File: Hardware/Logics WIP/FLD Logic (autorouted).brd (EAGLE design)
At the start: 62.2 x 33 mm, 86 parts

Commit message: 
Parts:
- removed H1, H2, H3, H4: MOUNT-HOLE3.3, holes:3,3
- moved C1 0.95 mm to (52.1, 4.45)
- moved C11 0.95 mm to (20.3, 10.8)
- moved C12 0.95 mm to (27.0, 9.21)
- moved C13 0.95 mm to (33.0, 10.8)
- moved C14 0.95 mm to (39.7, 9.21)
- moved C15 0.95 mm to (45.7, 10.8)
- moved C16 0.95 mm to (52.4, 9.21)
- moved C17 0.95 mm to (52.1, 17.1)
- moved C18 0.95 mm to (46.0, 15.6)
- moved C19 0.95 mm to (39.4, 17.1)
- moved C2 0.95 mm to (46.0, 2.86), turned to 180 degrees
- moved C20 0.95 mm to (33.3, 15.6)
- moved C21 0.95 mm to (26.7, 17.1)
- moved C22 0.95 mm to (20.6, 15.6)
- moved C23 0.95 mm to (14.0, 17.1)
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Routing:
- net +5V: track 460.1 -> 431.1 mm, vias 39 -> 40
- net DOUT: track 53.1 -> 28.5 mm, vias 3 -> 1
- net GND: track 360.7 -> 343.3 mm, vias 41 -> 40
- net N$36: track 24.8 -> 13.2 mm, vias 2 -> 0
- net N$37: track 13.2 -> 18.9 mm, vias 0 -> 2
- net N$7: track 12.2 -> 7.75 mm, vias 2 -> 0
- net N$6: track 11.5 -> 15.4 mm
- net N$25: track 12.5 -> 9.08 mm
- net N$11: track 18.7 -> 16.1 mm, vias 2 -> 0
- net N$34: track 7.79 -> 10.1 mm
- net N$8: track 11.0 -> 12.6 mm, vias 2 -> 0
- net N$15: track 12.5 -> 11.2 mm, vias 0 -> 2
- net N$19: track 17.4 -> 16.1 mm, vias 2 -> 0
- net N$20: track 13.2 -> 14.4 mm, vias 0 -> 2
- net N$26: track 12.4 -> 11.2 mm, vias 0 -> 2
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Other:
- board size 62.2 x 33 mm -> 61.6 x 33 mm
- board text added: "+ -"

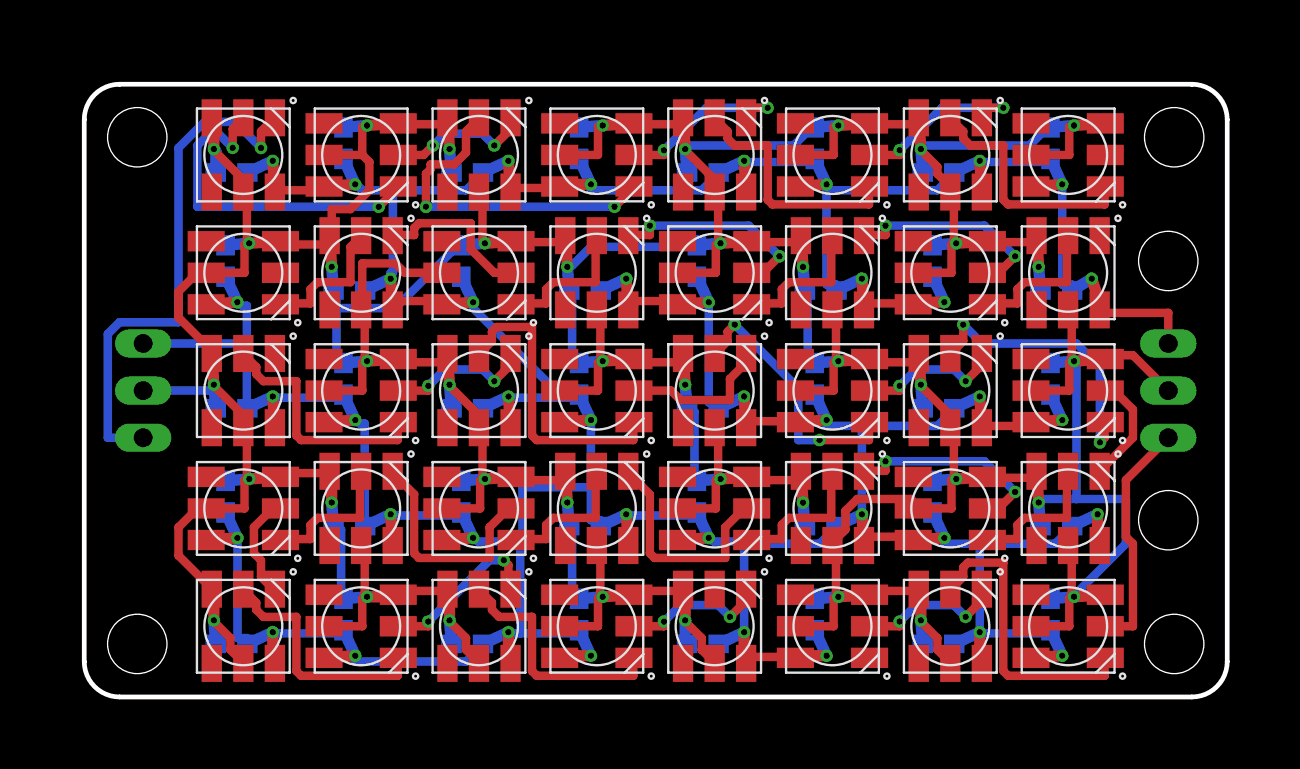
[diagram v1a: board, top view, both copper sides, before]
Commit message: 
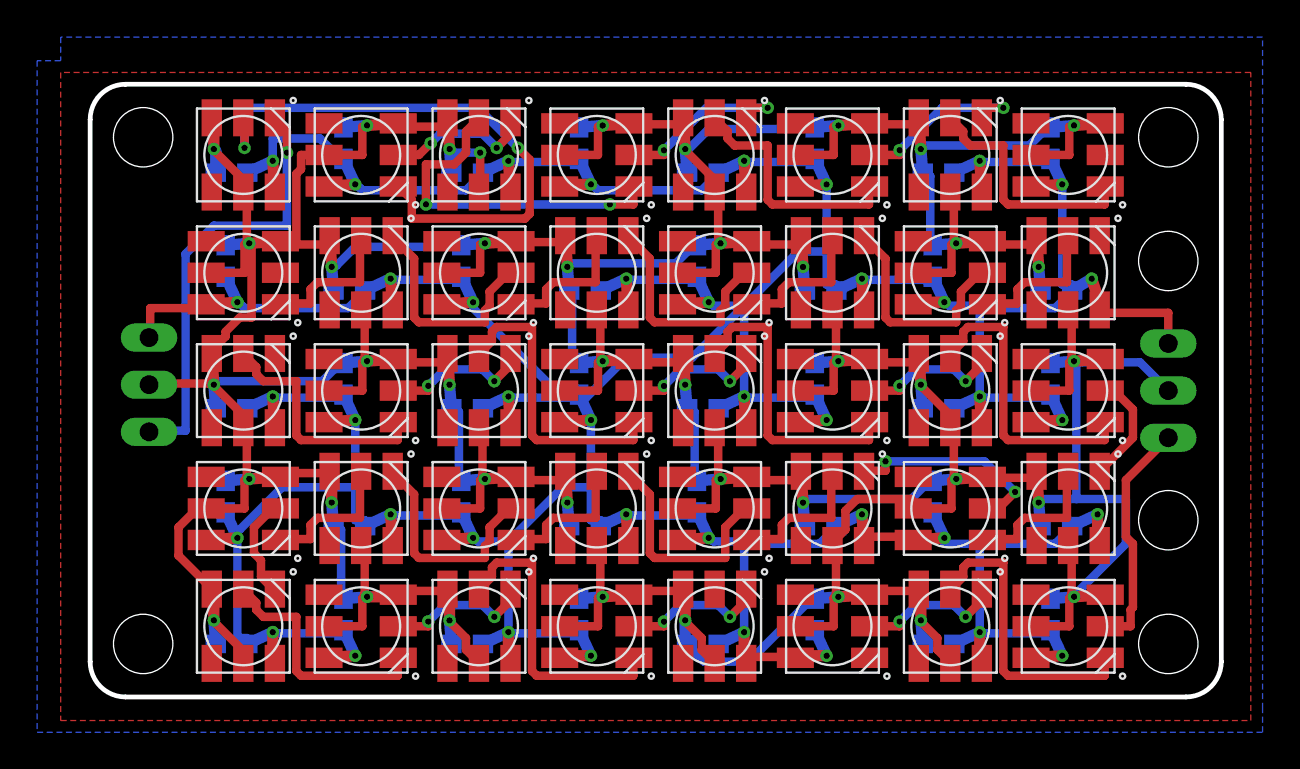
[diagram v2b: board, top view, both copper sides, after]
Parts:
- added U$1: (no value), rseries:RSERIES-OSHW-LOGO-SMALL
- moved OUT 0.45 mm to (3.49, 16.8)
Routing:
- net +5V: track 431.1 -> 445.4 mm, vias 40 -> 41
- net N$37: track 18.9 -> 31.7 mm
- net GND: track 343.3 -> 355.3 mm
- net DOUT: track 28.5 -> 23.7 mm
- net N$25: track 9.08 -> 12.4 mm
- net N$2: track 13.2 -> 16.1 mm
- net N$20: track 14.4 -> 16.1 mm, vias 2 -> 0
- net N$30: track 11.2 -> 12.4 mm, vias 2 -> 0
- net N$26: track 11.2 -> 12.4 mm, vias 2 -> 0
- net N$5: track 9.05 -> 7.92 mm
- net N$6: track 15.4 -> 16.1 mm, vias 2 -> 0
- net N$18: track 8.26 -> 7.92 mm, vias 0 -> 2
- added copper zone on layer 1, net GND
- added copper zone on layer 16, net GND
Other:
- board size 61.6 x 33 mm -> 61 x 33 mm
- board text added: "`VULCAN' FRONT LOGIC DISPLAY 2013-08-28"

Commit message: 
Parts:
- moved U$1 0.32 mm to (6.99, 28.3)
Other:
- board text added: "PROTOTYPE1"
- board text added: "`VULCAN' FRONT LOGIC DISPLAY : 2013-08-28"
- board text removed: "`VULCAN' FRONT LOGIC DISPLAY 2013-08-28"
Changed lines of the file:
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@@
 <setting verticaltext="up"/>
 </settings>
-<grid distance="0.025" unitdist="inch" unit="inch" style="lines" multiple="1" display="yes" altdistance="0.025" altunitdist="inch" altunit="inch"/>
+<grid distance="0.0125" unitdist="inch" unit="inch" style="lines" multiple="1" display="yes" altdistance="0.025" altunitdist="inch" altunit="inch"/>
 <layers>
 <layer number="1" name="Top" color="4" fill="1" visible="yes" active="yes"/>
@@
 <layer number="116" name="Patch_BOT" color="9" fill="4" visible="yes" active="yes"/>
 <layer number="121" name="_tsilk" color="7" fill="1" visible="yes" active="yes"/>
-<layer number="122" name="_bsilk" color="7" fill="1" visible="yes" active="yes"/>
+<layer number="122" name="bSilk" color="7" fill="1" visible="yes" active="yes"/>
 <layer number="123" name="tTestmark" color="7" fill="1" visible="yes" active="yes"/>
 <layer number="124" name="bTestmark" color="7" fill="1" visible="yes" active="yes"/>
@@
 <layer number="132" name="bAdjust" color="7" fill="1" visible="yes" active="yes"/>
 <layer number="144" name="Drill_legend" color="7" fill="1" visible="yes" active="yes"/>
-<layer number="150" name="Notes" color="7" fill="1" visible="yes" active="yes"/>
 <layer number="151" name="HeatSink" color="7" fill="1" visible="yes" active="yes"/>
 <layer number="153" name="FabDoc1" color="6" fill="1" visible="no" active="no"/>
@@
 <board>
 <plain>
-<wire x1="0.3175" y1="1.905" x2="0.3175" y2="31.115" width="0.254" layer="20"/>
-<wire x1="0.3175" y1="31.115" x2="2.2225" y2="33.02" width="0.254" layer="20" curve="-90"/>
-<wire x1="2.2225" y1="33.02" x2="59.3725" y2="33.02" width="0.254" layer="20"/>
-<wire x1="59.3725" y1="33.02" x2="61.2775" y2="31.115" width="0.254" layer="20" curve="-90"/>
-<wire x1="61.2775" y1="31.115" x2="61.2775" y2="1.905" width="0.254" layer="20"/>
-<wire x1="61.2775" y1="1.905" x2="59.3725" y2="0" width="0.254" layer="20" curve="-90"/>
-<wire x1="59.3725" y1="0" x2="2.2225" y2="0" width="0.254" layer="20"/>
-<wire x1="2.2225" y1="0" x2="0.3175" y2="1.905" width="0.254" layer="20" curve="-90"/>
+<wire x1="0.3175" y1="1.905" x2="0.3175" y2="31.115" width="0" layer="20"/>
+<wire x1="0.3175" y1="31.115" x2="2.2225" y2="33.02" width="0" layer="20" curve="-90"/>
+<wire x1="2.2225" y1="33.02" x2="59.3725" y2="33.02" width="0" layer="20"/>
+<wire x1="59.3725" y1="33.02" x2="61.2775" y2="31.115" width="0" layer="20" curve="-90"/>
+<wire x1="61.2775" y1="31.115" x2="61.2775" y2="1.905" width="0" layer="20"/>
+<wire x1="61.2775" y1="1.905" x2="59.3725" y2="0" width="0" layer="20" curve="-90"/>
+<wire x1="59.3725" y1="0" x2="2.2225" y2="0" width="0" layer="20"/>
+<wire x1="2.2225" y1="0" x2="0.3175" y2="1.905" width="0" layer="20" curve="-90"/>
 <hole x="58.42" y="30.1625" drill="3.2"/>
 <hole x="58.42" y="2.8575" drill="3.2"/>
@@
 <text x="61.2775" y="19.84375" size="1.397" layer="26" font="vector" rot="MR270">+ -</text>
 <text x="1.905" y="20.16125" size="1.397" layer="26" font="vector" rot="MR270">+ -</text>
-<text x="26.9875" y="25.4" size="1.016" layer="122" font="vector" rot="MR0" align="center">`VULCAN' FRONT LOGIC DISPLAY
-2013-08-28</text>
+<text x="24.13" y="32.0675" size="1.016" layer="26" font="vector" rot="MR0" align="center">`VULCAN' FRONT LOGIC DISPLAY : 2013-08-28</text>
+<polygon width="0" layer="26">
+<vertex x="16.4465" y="19.177"/>
+<vertex x="16.9545" y="15.875"/>
+<vertex x="18.2245" y="12.827"/>
+<vertex x="18.4785" y="11.811"/>
+<vertex x="18.9865" y="11.303"/>
+<vertex x="19.7485" y="11.557"/>
+<vertex x="20.0025" y="12.319"/>
+<vertex x="18.7325" y="15.367"/>
+<vertex x="17.9705" y="17.145"/>
+<vertex x="17.7165" y="19.177"/>
+<vertex x="18.2245" y="20.701"/>
+<vertex x="19.4945" y="20.955"/>
+<vertex x="20.7645" y="20.193"/>
+<vertex x="21.7805" y="18.923"/>
+<vertex x="22.2885" y="18.161"/>
+<vertex x="23.0505" y="18.415"/>
+<vertex x="23.3045" y="19.177"/>
+<vertex x="23.0505" y="20.193"/>
+<vertex x="22.0345" y="21.463"/>
+<vertex x="21.0185" y="22.225"/>
+<vertex x="20.0025" y="22.479"/>
+<vertex x="18.2245" y="22.225"/>
+<vertex x="16.9545" y="20.955"/>
+</polygon>
+<polygon width="0" layer="26">
+<vertex x="28.1305" y="3.175"/>
+<vertex x="27.6225" y="2.667"/>
+<vertex x="26.3525" y="2.413"/>
+<vertex x="23.8125" y="2.413"/>
+<vertex x="23.0505" y="2.667"/>
+<vertex x="22.2885" y="2.413"/>
+<vertex x="22.0345" y="1.905"/>
+<vertex x="22.2885" y="1.397"/>
+<vertex x="23.3045" y="1.143"/>
+<vertex x="27.1145" y="1.651"/>
+<vertex x="28.8925" y="2.413"/>
+<vertex x="29.6545" y="3.683"/>
+<vertex x="29.4005" y="4.953"/>
+<vertex x="28.6385" y="6.223"/>
+<vertex x="26.6065" y="8.001"/>
+<vertex x="26.0985" y="8.509"/>
+<vertex x="24.8285" y="10.287"/>
+<vertex x="23.8125" y="12.573"/>
+<vertex x="23.3045" y="14.605"/>
+<vertex x="23.3045" y="16.637"/>
+<vertex x="22.7965" y="16.891"/>
+<vertex x="22.0345" y="16.383"/>
+<vertex x="21.7805" y="15.113"/>
+<vertex x="22.0345" y="12.827"/>
+<vertex x="23.0505" y="9.779"/>
+<vertex x="24.5745" y="7.493"/>
+<vertex x="27.1145" y="4.953"/>
+</polygon>
+<polygon width="0" layer="26">
+<vertex x="9.5885" y="13.335"/>
+<vertex x="10.0965" y="12.319"/>
+<vertex x="11.1125" y="12.065"/>
+<vertex x="11.8745" y="10.287"/>
+<vertex x="12.1285" y="9.525"/>
+<vertex x="11.6205" y="8.763"/>
+<vertex x="10.3505" y="7.493"/>
+<vertex x="9.5885" y="6.985"/>
+<vertex x="8.3185" y="5.461"/>
+<vertex x="7.8105" y="3.683"/>
+<vertex x="8.3185" y="2.413"/>
+<vertex x="9.5885" y="1.905"/>
+<vertex x="12.1285" y="2.159"/>
+<vertex x="12.8905" y="2.413"/>
+<vertex x="13.1445" y="3.429"/>
+<vertex x="12.6365" y="3.937"/>
+<vertex x="10.0965" y="3.937"/>
+<vertex x="9.0805" y="4.445"/>
+<vertex x="10.0965" y="5.969"/>
+<vertex x="11.6205" y="7.239"/>
+<vertex x="12.3825" y="8.001"/>
+<vertex x="12.3825" y="8.255"/>
+<vertex x="13.6525" y="8.509"/>
+<vertex x="15.1765" y="8.255"/>
+<vertex x="16.4465" y="7.493"/>
+<vertex x="17.2085" y="8.255"/>
+<vertex x="17.2085" y="9.017"/>
+<vertex x="16.4465" y="9.779"/>
+<vertex x="14.9225" y="10.287"/>
+<vertex x="13.1445" y="10.541"/>
+<vertex x="13.1445" y="10.795"/>
+<vertex x="12.8905" y="12.065"/>
+<vertex x="15.4305" y="11.049"/>
+<vertex x="18.4785" y="10.033"/>
+<vertex x="19.2405" y="10.287"/>
+<vertex x="19.4945" y="11.049"/>
+<vertex x="18.9865" y="11.303"/>
+<vertex x="18.2245" y="11.557"/>
+<vertex x="16.1925" y="12.319"/>
+<vertex x="13.3985" y="13.589"/>
+<vertex x="10.6045" y="14.351"/>
+<vertex x="9.8425" y="14.097"/>
+</polygon>
+<polygon width="0" layer="26">
+<vertex x="12.6365" y="22.733"/>
+<vertex x="11.6205" y="22.479"/>
+<vertex x="11.3665" y="21.717"/>
+<vertex x="9.8425" y="18.669"/>
+<vertex x="9.0805" y="16.891"/>
+<vertex x="9.5885" y="16.637"/>
+<vertex x="8.5725" y="14.351"/>
+<vertex x="8.0645" y="13.335"/>
+<vertex x="8.3185" y="12.827"/>
+<vertex x="9.3345" y="13.589"/>
+<vertex x="15.1765" y="25.273"/>
+<vertex x="16.7005" y="27.051"/>
+<vertex x="18.7325" y="27.813"/>
+<vertex x="21.0185" y="27.813"/>
+<vertex x="23.0505" y="27.051"/>
+<vertex x="24.3205" y="25.273"/>
+<vertex x="24.8285" y="23.495"/>
+<vertex x="20.7645" y="25.527"/>
+<vertex x="16.4465" y="26.543"/>
+<vertex x="15.6845" y="24.003"/>
+<vertex x="16.9545" y="24.003"/>
+<vertex x="16.9545" y="24.257"/>
+<vertex x="16.7005" y="24.257"/>
+<vertex x="16.1925" y="24.765"/>
+<vertex x="16.1925" y="25.527"/>
+<vertex x="16.7005" y="26.035"/>
+<vertex x="17.2085" y="26.035"/>
+<vertex x="17.7165" y="25.527"/>
+<vertex x="17.7165" y="24.765"/>
+<vertex x="16.9545" y="24.257"/>
+<vertex x="16.9545" y="24.003"/>
+<vertex x="17.9705" y="24.003"/>
+<vertex x="22.2885" y="22.733"/>
+<vertex x="25.8445" y="21.209"/>
+<vertex x="26.6065" y="20.955"/>
+<vertex x="27.1145" y="20.701"/>
+<vertex x="27.8765" y="20.447"/>
+<vertex x="28.6385" y="20.447"/>
+<vertex x="27.3685" y="21.463"/>
+<vertex x="25.8445" y="22.225"/>
+<vertex x="26.0985" y="22.479"/>
+<vertex x="28.6385" y="21.209"/>
+<vertex x="29.4005" y="20.701"/>
+<vertex x="27.8765" y="21.717"/>
+<vertex x="26.0985" y="22.479"/>
+<vertex x="26.0985" y="24.765"/>
+<vertex x="25.5905" y="26.289"/>
+<vertex x="24.8285" y="27.559"/>
+<vertex x="22.7965" y="28.829"/>
+<vertex x="20.5105" y="29.337"/>
+<vertex x="18.2245" y="29.083"/>
+<vertex x="16.9545" y="28.575"/>
+<vertex x="14.9225" y="27.051"/>
+<vertex x="13.6525" y="25.019"/>
+<vertex x="12.3825" y="22.733"/>
+</polygon>
+<text x="46.0375" y="0.3175" size="1.778" layer="26" font="vector" rot="MR0">PROTOTYPE1</text>
 </plain>
 <attributes>
@@
 <attribute name="VALUE" x="6.6675" y="20.6375" size="1.27" layer="28" rot="MR270"/>
 </element>
-<element name="U$1" library="rseries" package="RSERIES-OSHW-LOGO-SMALL" value="" x="6.985" y="27.94" rot="MR270"/>
+<element name="U$1" library="rseries" package="RSERIES-OSHW-LOGO-SMALL" value="" x="6.985" y="28.2575" smashed="yes" rot="MR270"/>
 </elements>
 <signals>
@@
 </board>
 </drawing>
-<compatibility>
-<note version="6.3" minversion="6.2.2" severity="warning">
-Since Version 6.2.2 text objects can contain more than one line,
-which will not be processed correctly with this version.
-</note>
-</compatibility>
 </eagle>
